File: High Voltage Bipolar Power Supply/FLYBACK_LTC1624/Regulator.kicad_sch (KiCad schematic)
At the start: 40 parts, among them J1 1715734, Q3 TIP120, Q4 TIP125, U2 LM317HV_TO-220, U3 LM337HV_TO220

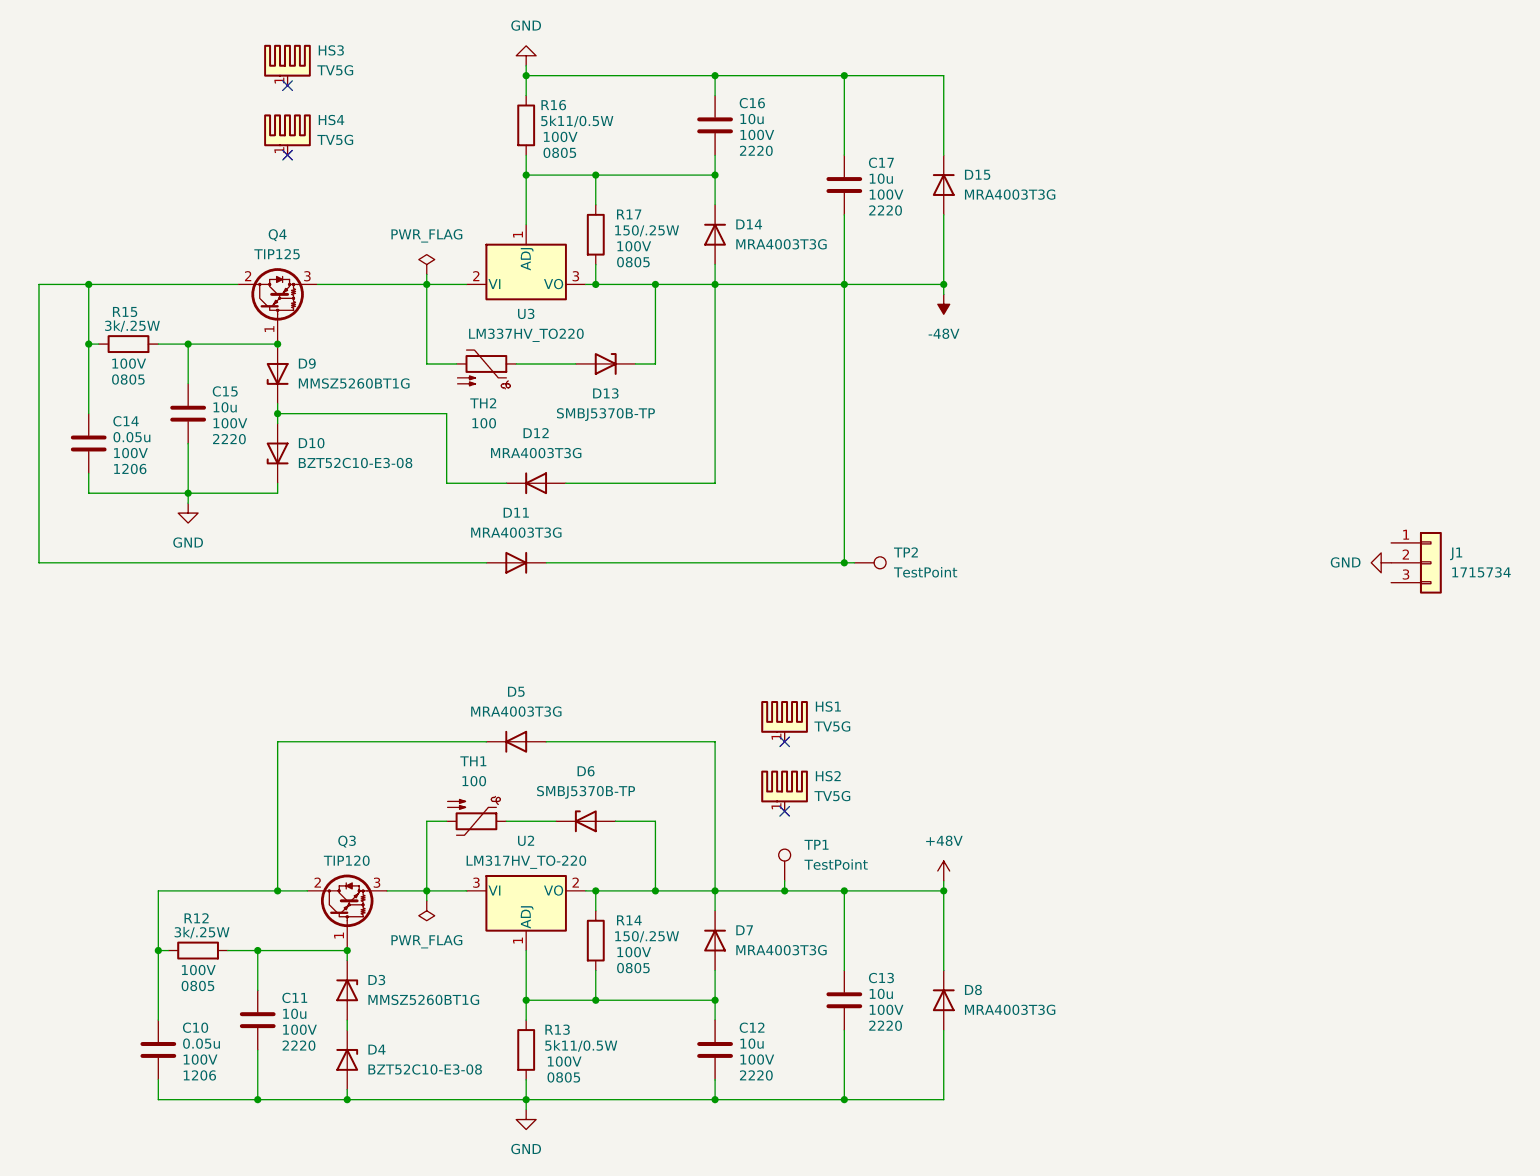
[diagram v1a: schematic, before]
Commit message: FLYBACK_LTC1624 : Schematic desing
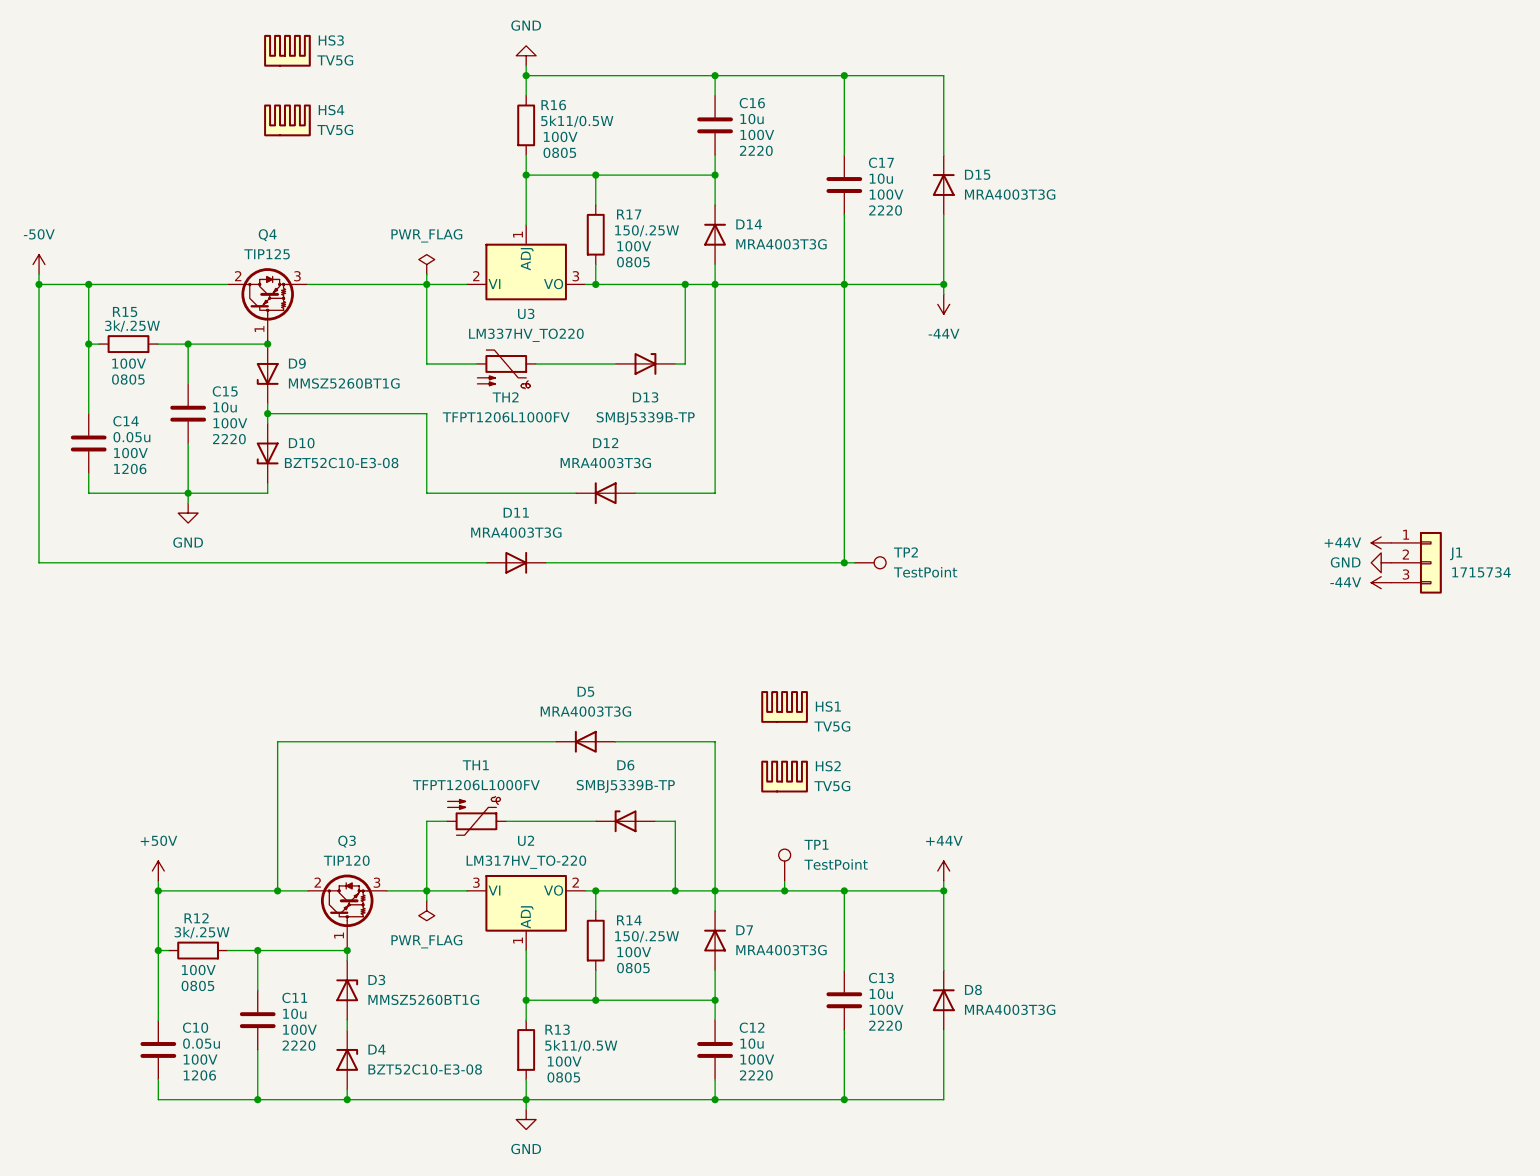
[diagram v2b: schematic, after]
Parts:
- D13, D6: value SMBJ5370B-TP -> SMBJ5339B-TP
- HS1, HS2, HS3, HS4: footprint FLYBACK_LT8304:Heatsink_AAVID_TV5G_TO220_Horizontal -> FLYBACK_LTC1624:Heatsink_AAVID_TV5G_TO220_Horizontal; symbol Mechanical:Heatsink_Pad -> Mechanical:Heatsink
- TH1, TH2: value 100 -> TFPT1206L1000FV; footprint (none) -> Resistor_SMD:R_1206_3216Metric_Pad1.30x1.75mm_HandSolder
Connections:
- net +48V is gone; now on net +44V: C13.1, D5.2 (A), D6.2 (A), D7.1 (K), D8.1 (K), R14.1, TP1.1, U2.2 (VO)
- net -48V is gone; now on net -44V: C17.2, D11.1 (K), D12.2 (A), D13.1 (K), D14.2 (A), D15.2 (A), R17.2, TP2.1, U3.3 (VO)
- net +44V: now reaches J1.1 (Pin_1)
- net -44V: now reaches J1.3 (Pin_3)
- net +50V: now reaches C10.1, D5.1 (K), Q3.2 (C), R12.1
- net -50V: now reaches C14.1, D11.2 (A), Q4.2 (C), R15.1
- no-connect marks 4 -> 0
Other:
- moved on the sheet: D10, D12, D13, D5, D6, D9, Q4, TH2

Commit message: FLYBACK_LTC1624: PCB layout
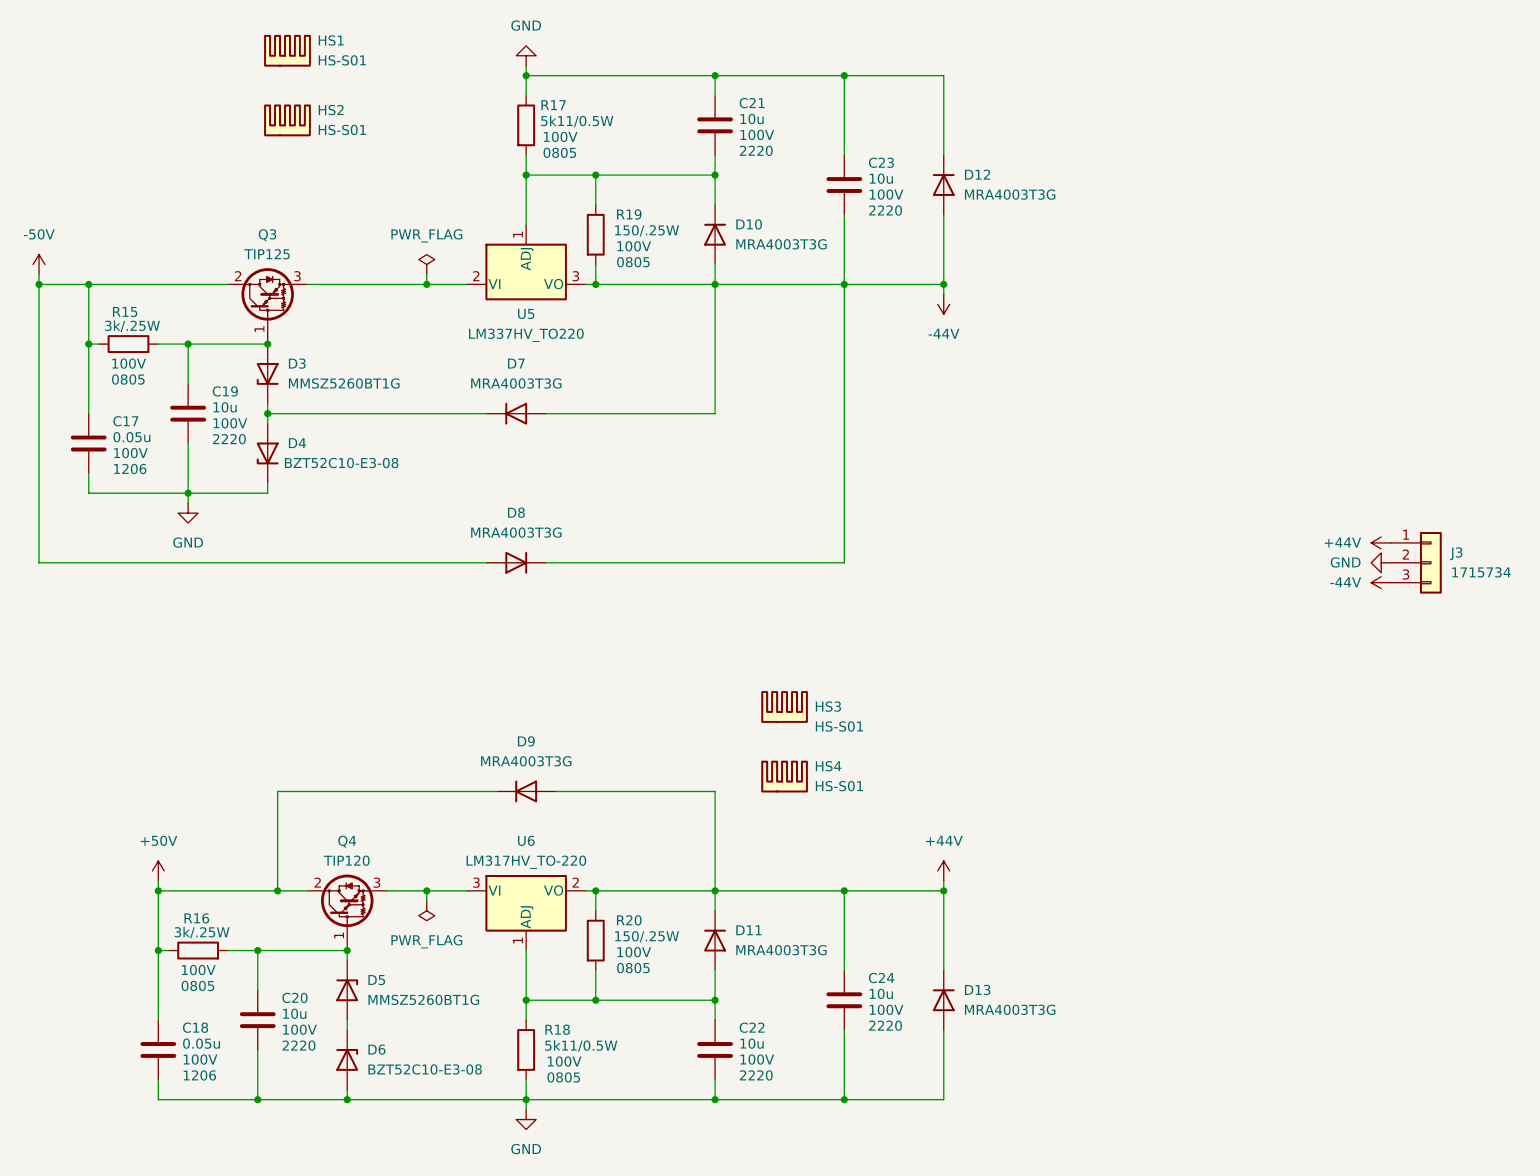
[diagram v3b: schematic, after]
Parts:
- removed D13, D6: SMBJ5339B-TP, Diode_SMD:D_SMB, symbol Device:D_Zener
- removed TH1, TH2: TFPT1206L1000FV, Resistor_SMD:R_1206_3216Metric_Pad1.30x1.75mm_HandSolder, symbol Device:Thermistor_PTC
- removed TP1, TP2: TestPoint, TestPoint:TestPoint_THTPad_D3.0mm_Drill1.5mm, symbol Connector:TestPoint
- C19: renamed from C15; footprint Capacitor_SMD:C_2220_5750Metric_Pad1.97x5.40mm_HandSolder -> FLYBACK_LTC1624:C_2220_5750Metric_Pad1.97x5.40mm_HandSolder
- C20: renamed from C11; footprint Capacitor_SMD:C_2220_5750Metric_Pad1.97x5.40mm_HandSolder -> FLYBACK_LTC1624:C_2220_5750Metric_Pad1.97x5.40mm_HandSolder
- C21: renamed from C16; footprint Capacitor_SMD:C_2220_5750Metric_Pad1.97x5.40mm_HandSolder -> FLYBACK_LTC1624:C_2220_5750Metric_Pad1.97x5.40mm_HandSolder
- C22: renamed from C12; footprint Capacitor_SMD:C_2220_5750Metric_Pad1.97x5.40mm_HandSolder -> FLYBACK_LTC1624:C_2220_5750Metric_Pad1.97x5.40mm_HandSolder
- C23: renamed from C17; footprint Capacitor_SMD:C_2220_5750Metric_Pad1.97x5.40mm_HandSolder -> FLYBACK_LTC1624:C_2220_5750Metric_Pad1.97x5.40mm_HandSolder
- C24: renamed from C13; footprint Capacitor_SMD:C_2220_5750Metric_Pad1.97x5.40mm_HandSolder -> FLYBACK_LTC1624:C_2220_5750Metric_Pad1.97x5.40mm_HandSolder
- HS1: renamed from HS3; value TV5G -> HS-S01; footprint FLYBACK_LTC1624:Heatsink_AAVID_TV5G_TO220_Horizontal -> FLYBACK_LTC1624:Heatsink_Stonecold_HS-S01_13.21x6.35mm
- HS2: renamed from HS4; value TV5G -> HS-S01; footprint FLYBACK_LTC1624:Heatsink_AAVID_TV5G_TO220_Horizontal -> FLYBACK_LTC1624:Heatsink_Stonecold_HS-S01_13.21x6.35mm
- HS3: renamed from HS1; value TV5G -> HS-S01; footprint FLYBACK_LTC1624:Heatsink_AAVID_TV5G_TO220_Horizontal -> FLYBACK_LTC1624:Heatsink_Stonecold_HS-S01_13.21x6.35mm
- HS4: renamed from HS2; value TV5G -> HS-S01; footprint FLYBACK_LTC1624:Heatsink_AAVID_TV5G_TO220_Horizontal -> FLYBACK_LTC1624:Heatsink_Stonecold_HS-S01_13.21x6.35mm
- Q3: renamed from Q4; footprint Package_TO_SOT_THT:TO-220-3_Horizontal_TabDown -> Package_TO_SOT_THT:TO-220-3_Vertical
- Q4: renamed from Q3; footprint Package_TO_SOT_THT:TO-220-3_Horizontal_TabDown -> Package_TO_SOT_THT:TO-220-3_Vertical
- U5: renamed from U3; footprint Package_TO_SOT_THT:TO-220-3_Horizontal_TabDown -> Package_TO_SOT_THT:TO-220-3_Vertical
- U6: renamed from U2; footprint Package_TO_SOT_THT:TO-220-3_Horizontal_TabDown -> Package_TO_SOT_THT:TO-220-3_Vertical
- renumbered C14 to C17, C10 to C18, D14 to D10, D7 to D11, D15 to D12, D8 to D13, D9 to D3, D10 to D4, D3 to D5, D4 to D6, D12 to D7, D11 to D8, D5 to D9, J1 to J3, R12 to R16, R16 to R17, R13 to R18, R17 to R19, R14 to R20
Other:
- moved on the sheet: D7, D9

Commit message: FLYBACK_LTC1624 : Design failed, can't buy LM377HV for -50V
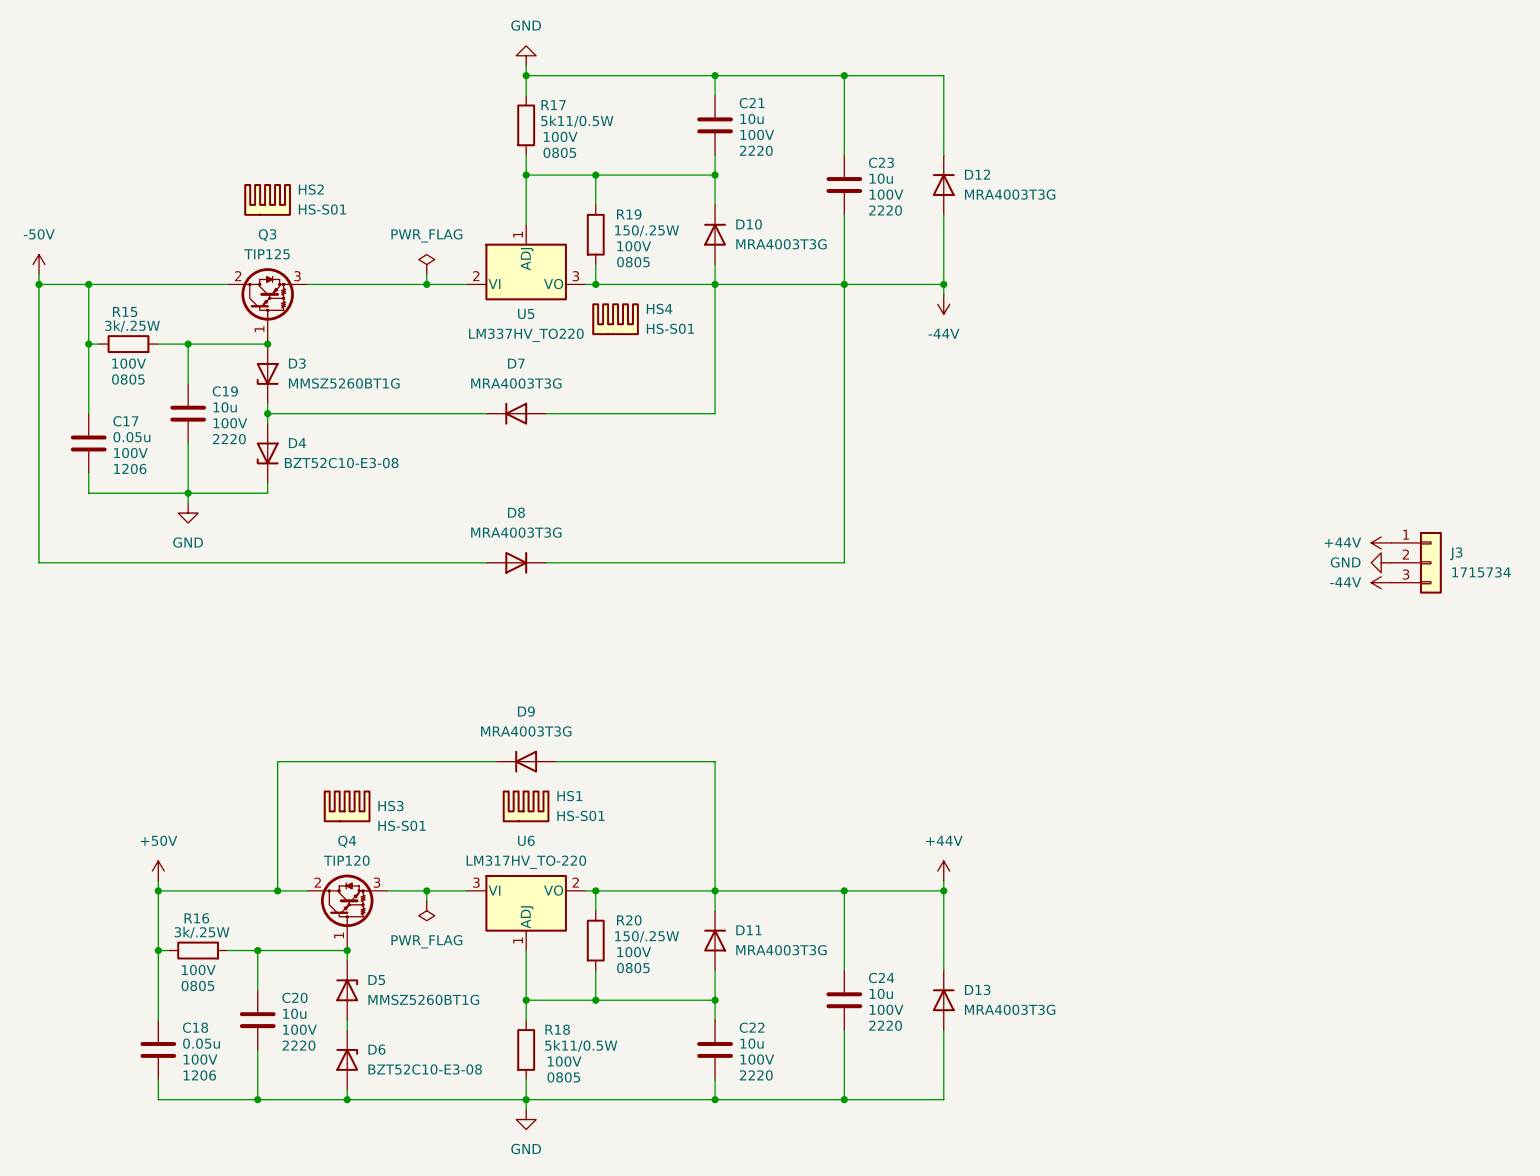
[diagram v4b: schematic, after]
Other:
- moved on the sheet: D9, HS1, HS2, HS3, HS4
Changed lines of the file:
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@@
 	(wire
 		(pts
-			(xy 134.62 115.57) (xy 154.94 115.57)
+			(xy 134.62 111.76) (xy 154.94 111.76)
 		)
 		(stroke
@@
 	(wire
 		(pts
-			(xy 99.06 115.57) (xy 99.06 128.27)
+			(xy 99.06 111.76) (xy 99.06 128.27)
 		)
 		(stroke
@@
 	(wire
 		(pts
-			(xy 127 115.57) (xy 99.06 115.57)
+			(xy 127 111.76) (xy 99.06 111.76)
 		)
 		(stroke
@@
 	(wire
 		(pts
-			(xy 154.94 115.57) (xy 154.94 128.27)
+			(xy 154.94 111.76) (xy 154.94 128.27)
 		)
 		(stroke
@@
 	(symbol
 		(lib_id "Device:D")
-		(at 130.81 115.57 0)
+		(at 130.81 111.76 0)
 		(unit 1)
 		(exclude_from_sim no)
@@
 		(fields_autoplaced yes)
 		(property "Reference" "D9"
-			(at 130.81 109.22 0)
+			(at 130.81 105.41 0)
 			(effects
 				(font
@@
 		)
 		(property "Value" "MRA4003T3G"
-			(at 130.81 111.76 0)
+			(at 130.81 107.95 0)
 			(effects
 				(font
@@
 		)
 		(property "Footprint" "Diode_SMD:D_SMA"
-			(at 130.81 115.57 0)
+			(at 130.81 111.76 0)
 			(effects
 				(font
@@
 		)
 		(property "Datasheet" "~"
-			(at 130.81 115.57 0)
+			(at 130.81 111.76 0)
 			(effects
 				(font
@@
 		)
 		(property "Description" "Diode"
-			(at 130.81 115.57 0)
+			(at 130.81 111.76 0)
 			(effects
 				(font
@@
 		)
 		(property "Sim.Device" "D"
-			(at 130.81 115.57 0)
+			(at 130.81 111.76 0)
 			(effects
 				(font
@@
 		)
 		(property "Sim.Pins" "1=K 2=A"
-			(at 130.81 115.57 0)
+			(at 130.81 111.76 0)
 			(effects
 				(font
@@
 	(symbol
 		(lib_id "Mechanical:Heatsink")
-		(at 100.33 31.75 0)
+		(at 97.79 41.91 0)
 		(unit 1)
 		(exclude_from_sim no)
@@
 		(fields_autoplaced yes)
 		(property "Reference" "HS2"
-			(at 104.14 28.5749 0)
+			(at 101.6 38.7349 0)
 			(effects
 				(font
@@
 		)
 		(property "Value" "HS-S01"
-			(at 104.14 31.1149 0)
+			(at 101.6 41.2749 0)
 			(effects
 				(font
@@
 		)
 		(property "Footprint" "FLYBACK_LTC1624:Heatsink_Stonecold_HS-S01_13.21x6.35mm"
-			(at 100.6348 31.75 0)
+			(at 98.0948 41.91 0)
 			(effects
 				(font
@@
 		)
 		(property "Datasheet" "~"
-			(at 100.6348 31.75 0)
+			(at 98.0948 41.91 0)
 			(effects
 				(font
@@
 		)
 		(property "Description" "Heatsink"
-			(at 100.33 31.75 0)
+			(at 97.79 41.91 0)
 			(effects
 				(font
@@
 	(symbol
 		(lib_id "Mechanical:Heatsink")
-		(at 163.83 115.57 0)
+		(at 142.24 57.15 0)
 		(unit 1)
 		(exclude_from_sim no)
@@
 		(fields_autoplaced yes)
 		(property "Reference" "HS4"
-			(at 167.64 112.3949 0)
+			(at 146.05 53.9749 0)
 			(effects
 				(font
@@
 		)
 		(property "Value" "HS-S01"
-			(at 167.64 114.9349 0)
+			(at 146.05 56.5149 0)
 			(effects
 				(font
@@
 		)
 		(property "Footprint" "FLYBACK_LTC1624:Heatsink_Stonecold_HS-S01_13.21x6.35mm"
-			(at 164.1348 115.57 0)
+			(at 142.5448 57.15 0)
 			(effects
 				(font
@@
 		)
 		(property "Datasheet" "~"
-			(at 164.1348 115.57 0)
+			(at 142.5448 57.15 0)
 			(effects
 				(font
@@
 		)
 		(property "Description" "Heatsink"
-			(at 163.83 115.57 0)
+			(at 142.24 57.15 0)
 			(effects
 				(font
@@
 	(symbol
 		(lib_id "Mechanical:Heatsink")
-		(at 163.83 106.68 0)
+		(at 107.95 119.38 0)
 		(unit 1)
 		(exclude_from_sim no)
@@
 		(dnp no)
 		(property "Reference" "HS3"
-			(at 167.64 104.7749 0)
+			(at 111.76 117.4749 0)
 			(effects
 				(font
@@
 		)
 		(property "Value" "HS-S01"
-			(at 167.64 107.3149 0)
+			(at 111.76 120.0149 0)
 			(effects
 				(font
@@
 		)
 		(property "Footprint" "FLYBACK_LTC1624:Heatsink_Stonecold_HS-S01_13.21x6.35mm"
-			(at 164.1348 106.68 0)
+			(at 108.2548 119.38 0)
 			(effects
 				(font
@@
 		)
 		(property "Datasheet" "~"
-			(at 164.1348 106.68 0)
+			(at 108.2548 119.38 0)
 			(effects
 				(font
@@
 		)
 		(property "Description" "Heatsink"
-			(at 163.83 106.68 0)
+			(at 107.95 119.38 0)
 			(effects
 				(font
@@
 	(symbol
 		(lib_id "Mechanical:Heatsink")
-		(at 100.33 22.86 0)
+		(at 130.81 119.38 0)
 		(unit 1)
 		(exclude_from_sim no)
@@
 		(fields_autoplaced yes)
 		(property "Reference" "HS1"
-			(at 104.14 19.6849 0)
+			(at 134.62 116.2049 0)
 			(effects
 				(font
@@
 		)
 		(property "Value" "HS-S01"
-			(at 104.14 22.2249 0)
+			(at 134.62 118.7449 0)
 			(effects
 				(font
@@
 		)
 		(property "Footprint" "FLYBACK_LTC1624:Heatsink_Stonecold_HS-S01_13.21x6.35mm"
-			(at 100.6348 22.86 0)
+			(at 131.1148 119.38 0)
 			(effects
 				(font
@@
 		)
 		(property "Datasheet" "~"
-			(at 100.6348 22.86 0)
+			(at 131.1148 119.38 0)
 			(effects
 				(font
@@
 		)
 		(property "Description" "Heatsink"
-			(at 100.33 22.86 0)
+			(at 130.81 119.38 0)
 			(effects
 				(font
